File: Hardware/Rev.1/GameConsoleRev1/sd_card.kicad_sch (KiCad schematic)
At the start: 3 parts, among them J13 Micro_SD_Card

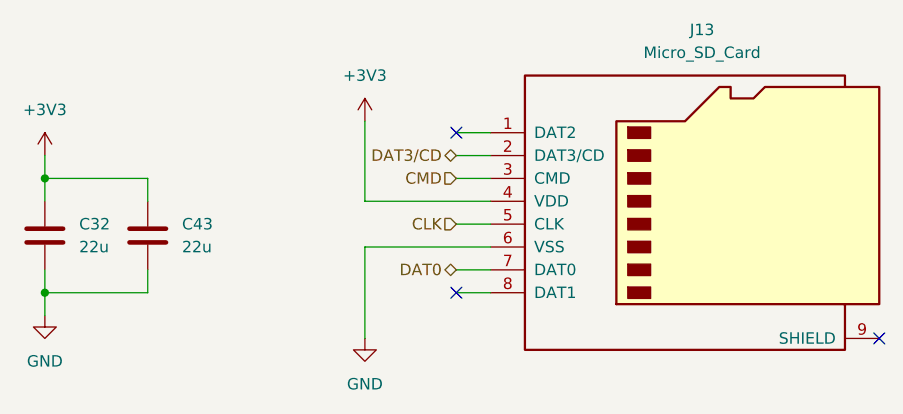
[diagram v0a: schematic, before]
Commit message: Added CPP Build
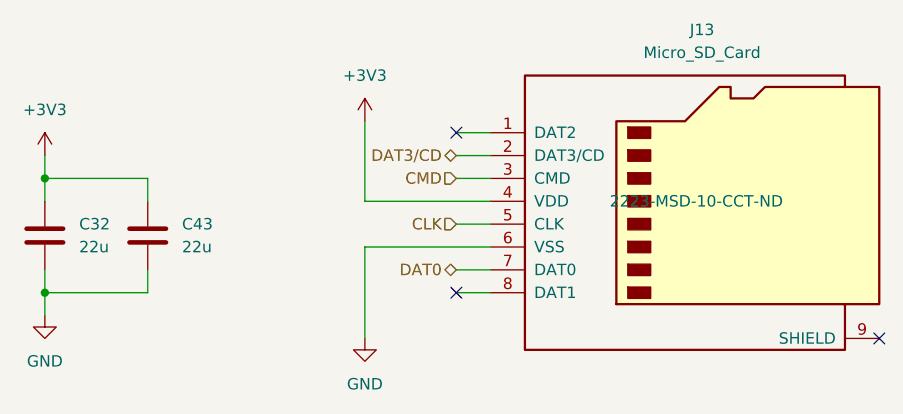
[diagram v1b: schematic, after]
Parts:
- J13: DK# (none) -> 2223-MSD-10-CCT-ND
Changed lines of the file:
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@@
+			)
+		)
+		(property "DK" ""
+			(at 69.85 90.17 0)
+			(effects
+				(font
+					(size 1.27 1.27)
+				)
 			)
 		)
@@
 			)
 		)
+		(property "DK" ""
+			(at 130.81 86.36 0)
+			(effects
+				(font
+					(size 1.27 1.27)
+				)
+			)
+		)
+		(property "DK#" "2223-MSD-10-CCT-ND"
+			(at 130.81 86.36 0)
+			(effects
+				(font
+					(size 1.27 1.27)
+				)
+			)
+		)
 		(pin "3"
 		)
@@
 			(at 58.42 90.17 0)
 			(effects
+				(font
+					(size 1.27 1.27)
+				)
+			)
+		)
+		(property "DK" ""
+			(at 58.42 90.17 0)
+			(effects
